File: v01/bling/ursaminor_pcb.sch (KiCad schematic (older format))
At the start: 135 parts, among them J1 USB_C_Receptacle_USB2.0, J2 I2C-L, J3 I2C-R, J4 AVR-ISP-6, SW1 Reset, U1 ATmega32U4-AU, U2 MCP23017_SO, U5 PRTR5V0U2X, U6 PRTR5V0U2X, U7 PRTR5V0U2X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

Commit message: Fix DRC and add jcl tag
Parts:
- U5, U6, U7: symbol keebio:PRTR5V0U2X -> ursaminor_pcb-rescue:PRTR5V0U2X-keebio
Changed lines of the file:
@@
 $EndComp
 $Comp
-L keebio:PRTR5V0U2X U5
+L ursaminor_pcb-rescue:PRTR5V0U2X-keebio U5
 U 1 1 6185F515
 P 6800 2250
@@
 Connection ~ 7200 1850
 $Comp
-L keebio:PRTR5V0U2X U6
+L ursaminor_pcb-rescue:PRTR5V0U2X-keebio U6
 U 1 1 620AFCBA
 P 7000 5000
@@
 	7400 4600 7450 4600
 $Comp
-L keebio:PRTR5V0U2X U7
+L ursaminor_pcb-rescue:PRTR5V0U2X-keebio U7
 U 1 1 621D90B5
 P 7100 7850
@@
 $EndComp
 $Comp
-L power:+5V #PWR?
+L power:+5V #PWR0155
 U 1 1 626B327C
 P 6550 5150
-F 0 "#PWR?" H 6550 5000 50  0001 C CNN
+F 0 "#PWR0155" H 6550 5000 50  0001 C CNN
 F 1 "+5V" H 6565 5323 50  0000 C CNN
 F 2 "" H 6550 5150 50  0001 C CNN

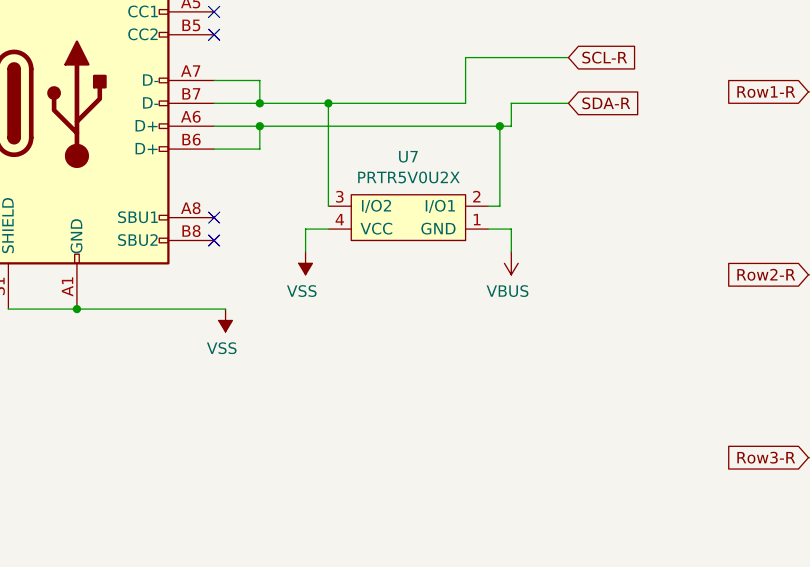
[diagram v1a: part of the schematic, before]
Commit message: Fix incorrectly wired ESD
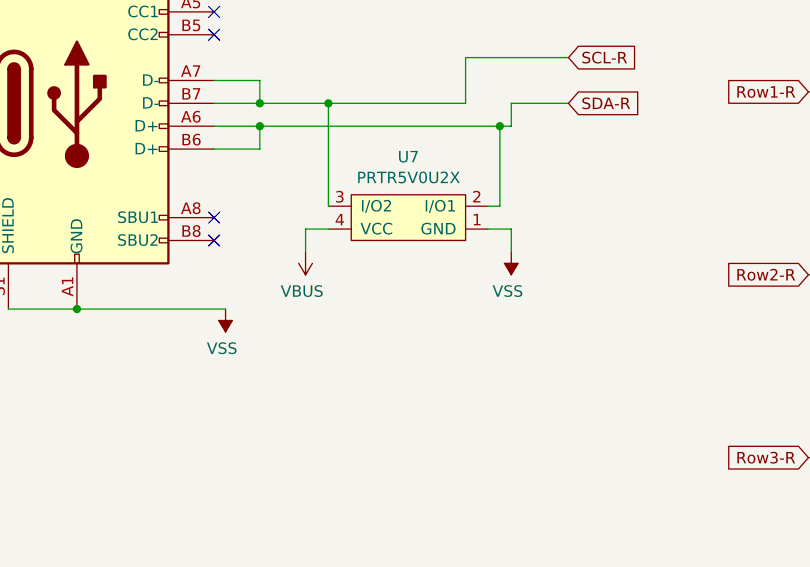
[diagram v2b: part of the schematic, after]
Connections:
- net VBUS: now also U7.4 (VCC); no longer U7.1 (GND)
- net VSS: now also U7.1 (GND); no longer U7.4 (VCC)
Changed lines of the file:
@@
 L power:VSS #PWR0157
 U 1 1 624A2AAA
+P 7550 8000
+F 0 "#PWR0157" H 7550 7850 50  0001 C CNN
+F 1 "VSS" H 7565 8173 50  0000 C CNN
+F 2 "" H 7550 8000 50  0001 C CNN
+F 3 "" H 7550 8000 50  0001 C CNN
+	1    7550 8000
+	-1   0    0    1
+$EndComp
+$Comp
+L power:VBUS #PWR0158
+U 1 1 624B2EFB
 P 6650 8000
-F 0 "#PWR0157" H 6650 7850 50  0001 C CNN
-F 1 "VSS" H 6665 8173 50  0000 C CNN
+F 0 "#PWR0158" H 6650 7850 50  0001 C CNN
+F 1 "VBUS" H 6665 8173 50  0000 C CNN
 F 2 "" H 6650 8000 50  0001 C CNN
 F 3 "" H 6650 8000 50  0001 C CNN
@@
 	-1   0    0    1
 $EndComp
-$Comp
-L power:VBUS #PWR0158
-U 1 1 624B2EFB
-P 7550 8000
-F 0 "#PWR0158" H 7550 7850 50  0001 C CNN
-F 1 "VBUS" H 7565 8173 50  0000 C CNN
-F 2 "" H 7550 8000 50  0001 C CNN
-F 3 "" H 7550 8000 50  0001 C CNN
-	1    7550 8000
-	-1   0    0    1
-$EndComp
